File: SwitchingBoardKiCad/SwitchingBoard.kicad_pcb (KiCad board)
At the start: 2 copper layers, 129.5 x 78.7 mm, 55 parts, among them J1 Screw_Terminal_01x02, J10 Fuse_, J11 Fuse, J2 Screw_Terminal_01x02, J3 Screw_Terminal_01x02, J4 Screw_Terminal_01x02, J5 Screw_Terminal_01x03, J6 Screw_Terminal_01x02, J7 Screw_Terminal_01x02, J8 Screw_Terminal_01x02, J9 Screw_Terminal_01x02, K1 FINDER-30.22, Q1 BT169G, Q2 BTB16-800CW, Q3 BTB16-800CW, U1 MOC3063M

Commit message: Removed optocoupler from this board and updated the fuseholder footprint.
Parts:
- removed the C2 at (67.3, 31.9)
- removed J10: Fuse_, TerminalBlock:TerminalBlock_bornier-2_P5.08mm
- removed J11: Fuse, TerminalBlock:TerminalBlock_bornier-2_P5.08mm
- removed U1: MOC3063M, Package_DIP:DIP-6_W7.62mm_LongPads
- added F1: Fuse, FuseHolders:Fuseholder_Clip-5x20mm&6.3x32_Schurter_OG_Lateral_P20.00x5.00mm_D1.3mm_Horizontal, F.Cu at (43.3, 28.1)
- moved C2 2.84 mm to (66.0, 38.2)
- renumbered C3 to C1, C11 to C10, C12 to C11, C13 to C12, C1 to C2, C4 to C3, C5 to C4, C6 to C5, C7 to C6, C8 to C7, C9 to C8, C10 to C9, D2 to D1, D1 to D2, R4 to R3, R5 to R4, R6 to R5, R3 to R6
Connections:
- D2 pad 2: Net-(D1-Pad2) -> Net-(D2-Pad2)
- K1 pad 14: unconnected-(K1-Pad14) -> /Timed live
- K1 pad 21: /Control Live -> unconnected-(K1-Pad21)
- K1 pad 24: /Timed live -> unconnected-(K1-Pad24)
- Q1 pad 2: Net-(Q1-Pad2) -> Net-(J3-Pad1)
- R2 pad 1: Net-(R2-Pad1) -> Net-(J3-Pad2)
- R3 pad 2: Net-(Q1-Pad2) -> Net-(J3-Pad1)
- R6 pad 1: /RL_PoleOneNC -> Net-(D2-Pad2)
- R6 pad 2: Net-(D1-Pad2) -> /RL_PoleOneNC

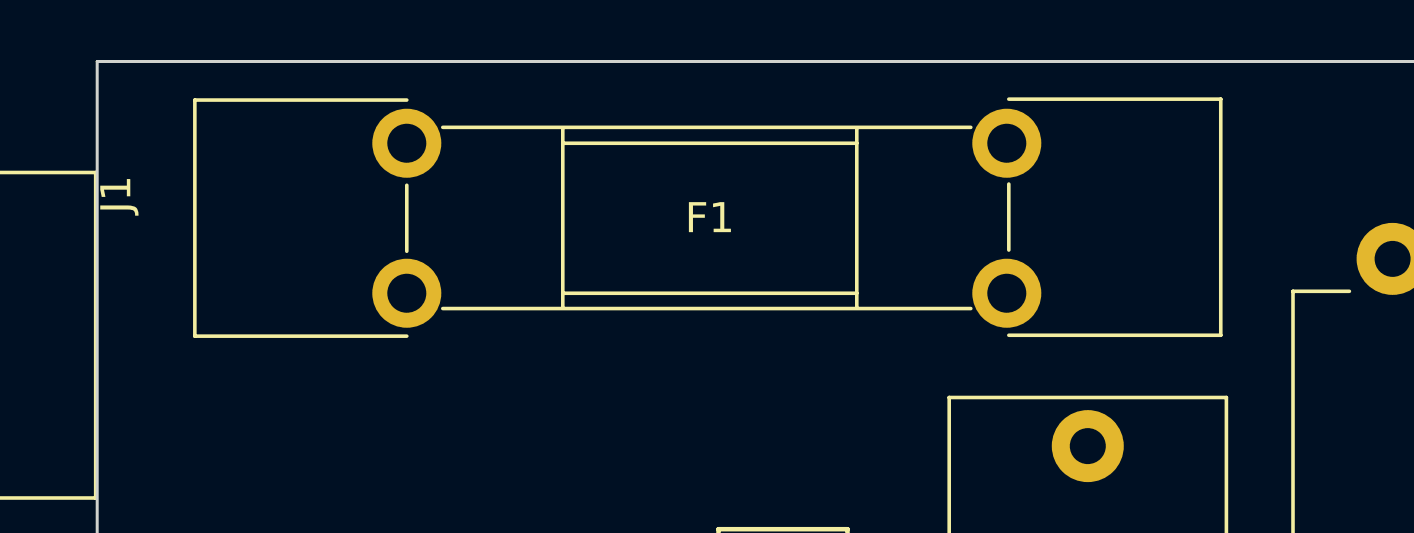
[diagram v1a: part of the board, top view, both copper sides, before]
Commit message: Added custom fuse footprint and updated PCB.
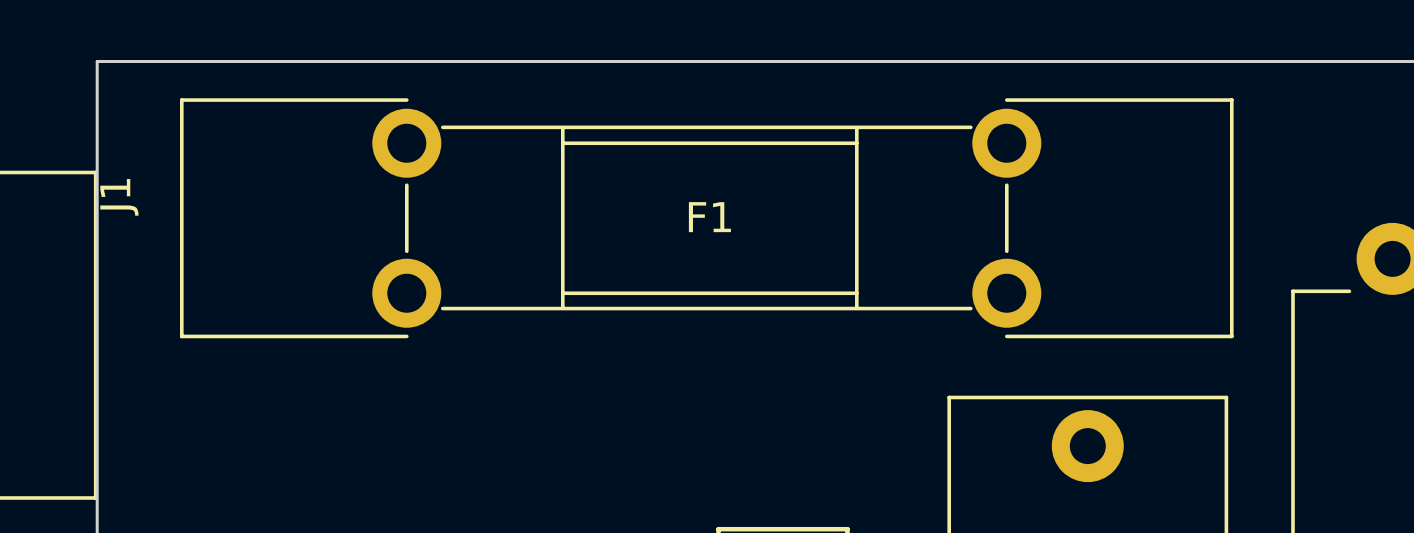
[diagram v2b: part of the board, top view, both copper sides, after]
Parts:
- F1: footprint FuseHolders:Fuseholder_Clip-5x20mm&6.3x32_Schurter_OG_Lateral_P20.00x5.00mm_D1.3mm_Horizontal -> ITFootprints:Fuseholder_Clip-5x20mmOr6.3x32_Schurter_OG_Lateral_P20.00x5.00mm_D1.3mm_Horizontal
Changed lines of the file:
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@@
     )
   )
-  (footprint "FuseHolders:Fuseholder_Clip-5x20mm&6.3x32_Schurter_OG_Lateral_P20.00x5.00mm_D1.3mm_Horizontal" (layer "F.Cu")
+  (footprint "ITFootprints:Fuseholder_Clip-5x20mmOr6.3x32_Schurter_OG_Lateral_P20.00x5.00mm_D1.3mm_Horizontal" (layer "F.Cu")
     (at 43.34 28.125)
     (descr "Fuseholder Clips, 5x20mm/6.3x32mm Cylinder Fuse, Pins Inline, Horizontal, Schurter OG, https://us.schurter.com/bundles/snceschurter/epim/_ProdPool_/newDS/en/typ_OG__Clip__5x20___6.3x32.pdf")
@@
       (effects (font (size 1 1) (thickness 0.15)))
     )
+    (fp_line (start 20 1.4) (end 20 3.6) (layer "F.SilkS") (width 0.12))
+    (fp_line (start -7.5 -1.44) (end -7.5 6.44) (layer "F.SilkS") (width 0.12))
+    (fp_line (start 20 -1.44) (end 27.5 -1.44) (layer "F.SilkS") (width 0.12))
+    (fp_line (start 18.8 -0.53) (end 1.2 -0.53) (layer "F.SilkS") (width 0.12))
+    (fp_line (start 0 3.6) (end 0 1.4) (layer "F.SilkS") (width 0.12))
+    (fp_line (start 0 6.44) (end -7.5 6.44) (layer "F.SilkS") (width 0.12))
+    (fp_line (start 27.5 6.44) (end 27.5 -1.44) (layer "F.SilkS") (width 0.12))
+    (fp_line (start 0 -1.44) (end -7.5 -1.44) (layer "F.SilkS") (width 0.12))
+    (fp_line (start 15 -0.5) (end 15 5.5) (layer "F.SilkS") (width 0.12))
+    (fp_line (start 18.8 5.51) (end 1.2 5.51) (layer "F.SilkS") (width 0.12))
+    (fp_line (start 20 6.44) (end 27.5 6.44) (layer "F.SilkS") (width 0.12))
     (fp_line (start 15 0) (end 5.2 0) (layer "F.SilkS") (width 0.12))
-    (fp_line (start 0 -1.44) (end -7.065 -1.44) (layer "F.SilkS") (width 0.12))
-    (fp_line (start 18.8 5.51) (end 1.2 5.51) (layer "F.SilkS") (width 0.12))
-    (fp_line (start 27.1325 6.4) (end 27.1325 -1.47) (layer "F.SilkS") (width 0.12))
-    (fp_line (start 15 -0.5) (end 15 5.5) (layer "F.SilkS") (width 0.12))
     (fp_line (start 5.2 -0.5) (end 5.2 5.5) (layer "F.SilkS") (width 0.12))
-    (fp_line (start 0 3.6) (end 0 1.4) (layer "F.SilkS") (width 0.12))
-    (fp_line (start 20.0675 6.4) (end 27.1325 6.4) (layer "F.SilkS") (width 0.12))
-    (fp_line (start 0 6.43) (end -7.065 6.43) (layer "F.SilkS") (width 0.12))
-    (fp_line (start 20.0675 1.36) (end 20.0675 3.56) (layer "F.SilkS") (width 0.12))
-    (fp_line (start 20.0675 -1.47) (end 27.1325 -1.47) (layer "F.SilkS") (width 0.12))
     (fp_line (start 15 5) (end 5.2 5) (layer "F.SilkS") (width 0.12))
-    (fp_line (start -7.065 -1.44) (end -7.065 6.43) (layer "F.SilkS") (width 0.12))
-    (fp_line (start 18.8 -0.53) (end 1.2 -0.53) (layer "F.SilkS") (width 0.12))
-    (fp_line (start 29.105 6.8) (end -9.105 6.8) (layer "F.CrtYd") (width 0.05))
-    (fp_line (start 29.105 6.8) (end 29.105 -2.09) (layer "F.CrtYd") (width 0.05))
-    (fp_line (start -9.105 -2.09) (end 29.105 -2.09) (layer "F.CrtYd") (width 0.05))
-    (fp_line (start -9.105 -2.09) (end -9.105 6.8) (layer "F.CrtYd") (width 0.05))
-    (fp_line (start 27.1325 6.4) (end 20.0675 6.4) (layer "F.Fab") (width 0.1))
-    (fp_line (start 20.0675 -1.47) (end 27.1325 -1.47) (layer "F.Fab") (width 0.1))
-    (fp_line (start -7.065 6.43) (end -7.065 -1.44) (layer "F.Fab") (width 0.1))
-    (fp_line (start -7.065 -1.44) (end 0 -1.44) (layer "F.Fab") (width 0.1))
+    (fp_line (start 29 6.965) (end -9 6.965) (layer "F.CrtYd") (width 0.05))
+    (fp_line (start -9 -1.965) (end 29 -1.965) (layer "F.CrtYd") (width 0.05))
+    (fp_line (start -9 -1.965) (end -9 6.965) (layer "F.CrtYd") (width 0.05))
+    (fp_line (start 29 6.965) (end 29 -1.965) (layer "F.CrtYd") (width 0.05))
+    (fp_line (start 20 -1.44) (end 27.5 -1.44) (layer "F.Fab") (width 0.1))
+    (fp_line (start 0 -1.44) (end -7.5 -1.44) (layer "F.Fab") (width 0.1))
+    (fp_line (start 15 -0.5) (end 15 5.5) (layer "F.Fab") (width 0.1))
+    (fp_line (start 20 6.44) (end 27.5 6.44) (layer "F.Fab") (width 0.1))
+    (fp_line (start 0 3.6) (end 0 1.4) (layer "F.Fab") (width 0.1))
+    (fp_line (start 27.5 6.44) (end 27.5 -1.44) (layer "F.Fab") (width 0.1))
+    (fp_line (start -7.5 -1.44) (end -7.5 6.44) (layer "F.Fab") (width 0.1))
     (fp_line (start 5.2 -0.5) (end 5.2 5.5) (layer "F.Fab") (width 0.1))
+    (fp_line (start 18.8 -0.53) (end 1.2 -0.53) (layer "F.Fab") (width 0.1))
+    (fp_line (start 20 1.4) (end 20 3.6) (layer "F.Fab") (width 0.1))
+    (fp_line (start 18.8 5.51) (end 1.2 5.51) (layer "F.Fab") (width 0.1))
+    (fp_line (start 15 0) (end 5.2 0) (layer "F.Fab") (width 0.1))
     (fp_line (start 15 5) (end 5.2 5) (layer "F.Fab") (width 0.1))
-    (fp_line (start 18.8 5.49) (end 1.2 5.49) (layer "F.Fab") (width 0.1))
-    (fp_line (start 5.2 0) (end 15 0) (layer "F.Fab") (width 0.1))
-    (fp_line (start 15 -0.5) (end 15 5.5) (layer "F.Fab") (width 0.1))
-    (fp_line (start 0 1.4) (end 0 3.6) (layer "F.Fab") (width 0.1))
-    (fp_line (start 1.2 -0.55) (end 18.8 -0.55) (layer "F.Fab") (width 0.1))
-    (fp_line (start 0 6.43) (end -7.065 6.43) (layer "F.Fab") (width 0.1))
-    (fp_line (start 20.0675 3.56) (end 20.0675 1.36) (layer "F.Fab") (width 0.1))
-    (fp_line (start 27.1325 -1.47) (end 27.1325 6.4) (layer "F.Fab") (width 0.1))
+    (fp_line (start 0 6.44) (end -7.5 6.44) (layer "F.Fab") (width 0.1))
+    (pad "1" thru_hole circle (at 0 5) (size 2.3 2.3) (drill 1.3) (layers *.Cu *.Mask)
+      (net 18 "/Live") (pintype "passive"))
     (pad "1" thru_hole circle (at 0 0) (size 2.3 2.3) (drill 1.3) (layers *.Cu *.Mask)
-      (net 18 "/Live") (pintype "passive"))
-    (pad "1" thru_hole circle (at 0 5) (size 2.3 2.3) (drill 1.3) (layers *.Cu *.Mask)
       (net 18 "/Live") (pintype "passive"))
     (pad "2" thru_hole circle (at 20 0) (size 2.3 2.3) (drill 1.3) (layers *.Cu *.Mask)
@@
     (pad "2" thru_hole circle (at 20 5) (size 2.3 2.3) (drill 1.3) (layers *.Cu *.Mask)
       (net 26 "/Control Live") (pintype "passive"))
-    (model "${KISYS3DMOD}/Fuse.3dshapes/Fuseholder_Clip-5x20mm_Schurter_OG_Lateral_P15.00x5.00mm_D1.3mm_Horizontal.wrl"
+    (model "${KISYS3DMOD}/Fuse.3dshapes/Fuseholder_Clip-5x20mmOr6.3x32_Schurter_OG_Lateral_P20.00x5.00mm_D1.3mm_Horizontal.wrl"
       (offset (xyz 0 0 0))
       (scale (xyz 1 1 1))

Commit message: Playing with layout and routing in KiCad
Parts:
- added D3: D_TVS_Filled, Diode_THT:D_DO-15_P12.70mm_Horizontal, F.Cu at (219.6, 58.7)
- JP1, JP2, JP3: footprint TerminalBlock:TerminalBlock_bornier-3_P5.08mm -> TerminalBlock_4Ucon:TerminalBlock_4Ucon_1x03_P3.50mm_Horizontal
- R10, R16, R5: value 39 -> 47
- moved R4 153.4 mm to (229.2, 20.9)
- moved D1 150.4 mm to (239.3, 25.7)
- moved R6 149.3 mm to (233.0, 25.9)
- moved J4 146.1 mm to (80.8, 32.4), turned to 180 degrees
- moved C2 145.6 mm to (211.1, 25.8)
- moved J6 139.0 mm to (244.4, 45.0)
- moved D2 125.1 mm to (226.6, 48.6)
- moved C4 121.3 mm to (212.0, 55.9)
- moved K1 111.6 mm to (86.7, 52.7), turned to 90 degrees
- moved C7 107.9 mm to (80.8, 52.4), turned to 180 degrees
- moved D4 97.5 mm to (80.9, 40.8), turned to -90 degrees
- moved C6 89.1 mm to (101.8, 94.8), turned to 90 degrees
- moved C8 87.5 mm to (96.1, 94.8), turned to 90 degrees
- moved J9 80.7 mm to (117.7, 93.3), turned to 180 degrees
- moved J3 80.4 mm to (154.2, 53.0)
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- renumbered D3 to D4, D4 to D5, D5 to D6, D6 to D7, J6 to J5, J5 to J6
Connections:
- J8 pad 1: Net-(J8-Pad1) -> Net-(R13-Pad1)
- J8 pad 2: Net-(J8-Pad2) -> Net-(Q3-Pad3)
- Q3 pad 3: Net-(J8-Pad1) -> Net-(Q3-Pad3)
- R13 pad 1: Net-(J8-Pad2) -> Net-(R13-Pad1)
- R14 pad 2: Net-(J8-Pad1) -> Net-(Q3-Pad3)
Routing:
- net /Live: track 0.00 -> 149.2 mm
- net /Inrush protection: track 0.00 -> 37.1 mm
- net /Protection short: track 0.00 -> 34.0 mm
- net Net-(Q3-Pad3): track 0.00 -> 32.4 mm
- net Net-(C11-Pad2): track 0.00 -> 28.6 mm
- net Net-(J5-Pad1): track 0.00 -> 21.6 mm, vias 0 -> 1
- net /Neutral: track 0.00 -> 19.8 mm
- net Net-(C6-Pad2): track 0.00 -> 18.7 mm
- net Net-(R13-Pad2): track 0.00 -> 11.5 mm
- net /Control Live: track 0.00 -> 10.5 mm
- net Net-(R13-Pad1): track 0.00 -> 8.91 mm
- net Net-(JP2-Pad2): track 0.00 -> 7.91 mm
- net Net-(J5-Pad2): track 0.00 -> 7.05 mm
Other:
- board size 129.5 x 78.7 mm -> 100 x 74.5 mm

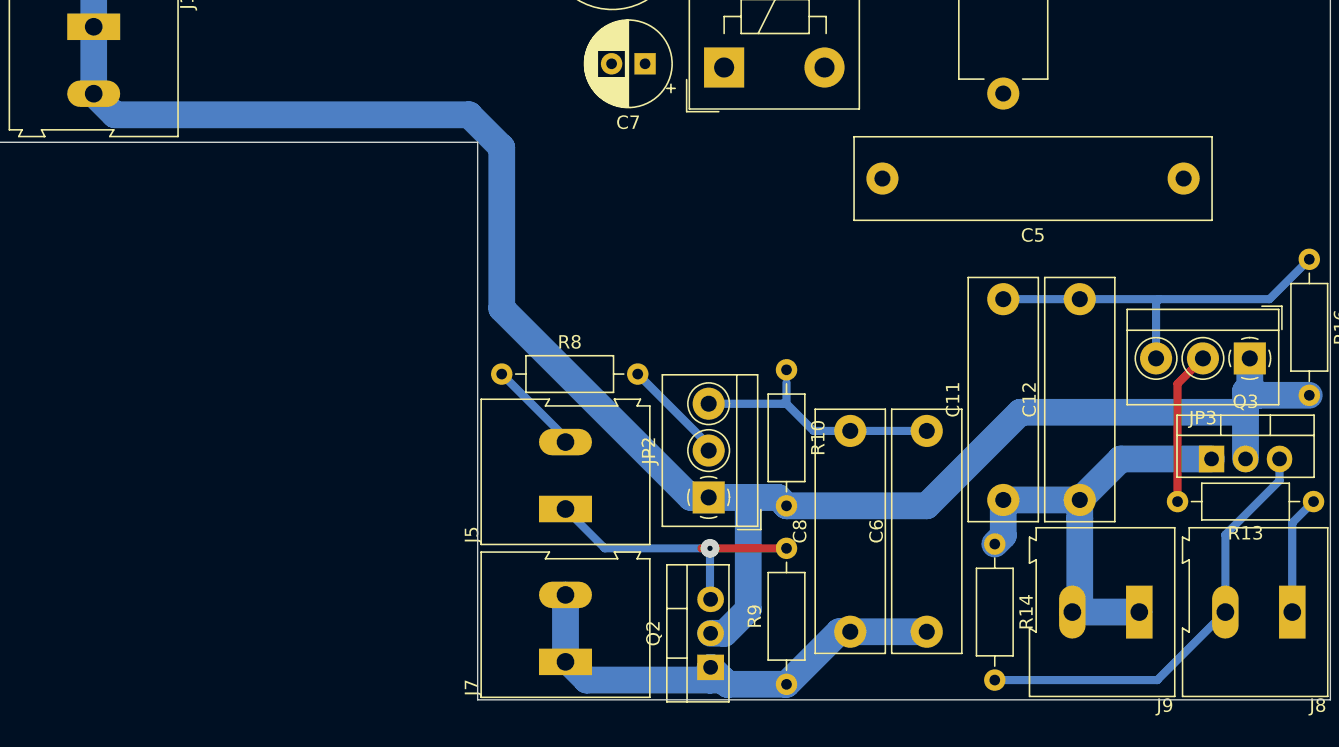
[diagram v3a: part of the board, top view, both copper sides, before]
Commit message: Shuffled component placement to avoid via.
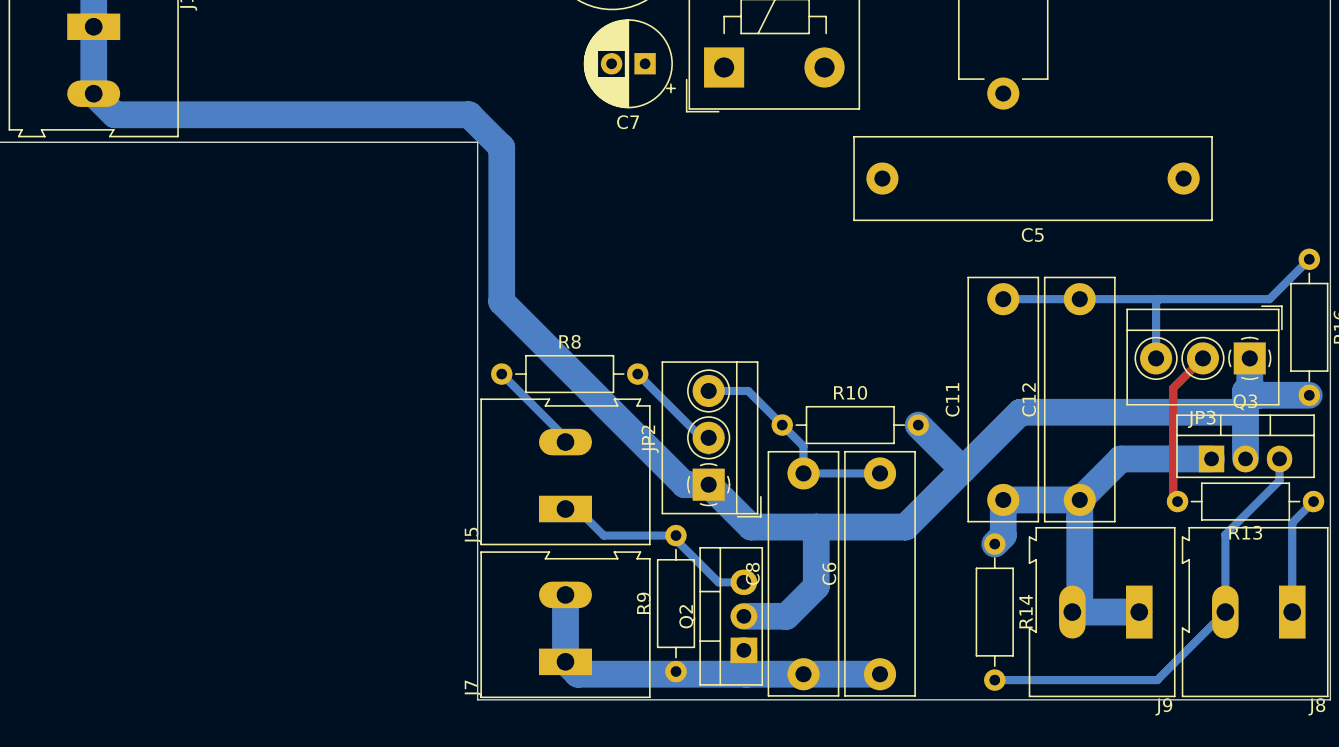
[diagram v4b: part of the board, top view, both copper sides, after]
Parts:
- moved R9 8.31 mm to (83.1, 97.8)
- moved C8 4.72 mm to (92.6, 98.0)
- moved C6 4.72 mm to (98.4, 98.0)
- moved R10 4.14 mm to (91.1, 79.4), turned to 0 degrees
- moved Q2 2.79 mm to (88.2, 96.2)
- moved JP2 0.95 mm to (85.6, 83.8)
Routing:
- net /Inrush protection: track 37.1 -> 31.0 mm
- net Net-(J5-Pad1): track 21.6 -> 16.3 mm, vias 1 -> 0
- net /Live: track 149.2 -> 153.5 mm
- net Net-(C6-Pad2): track 18.7 -> 16.5 mm
